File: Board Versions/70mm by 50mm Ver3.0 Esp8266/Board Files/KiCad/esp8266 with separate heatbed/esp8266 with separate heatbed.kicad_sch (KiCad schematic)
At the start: 11 parts

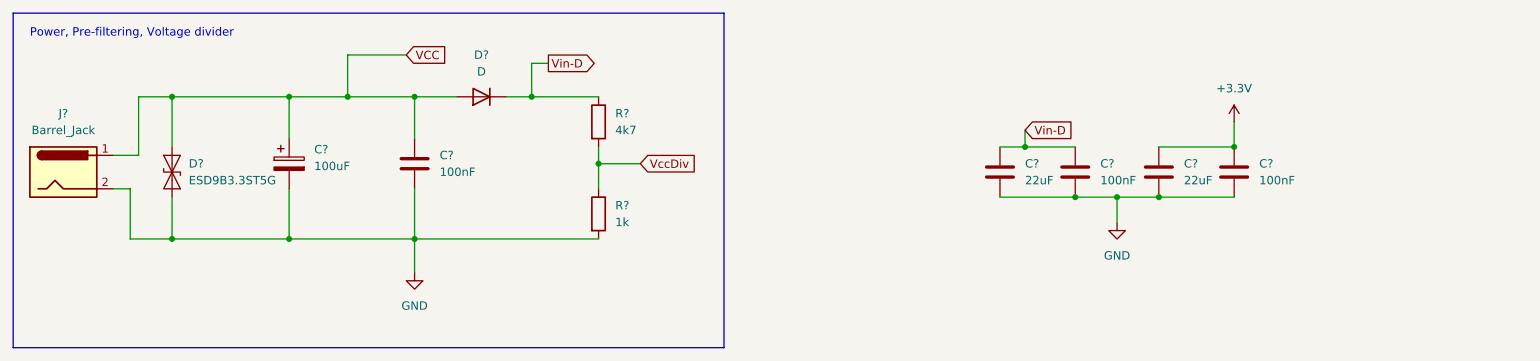
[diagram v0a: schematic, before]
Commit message: LDO + temperature
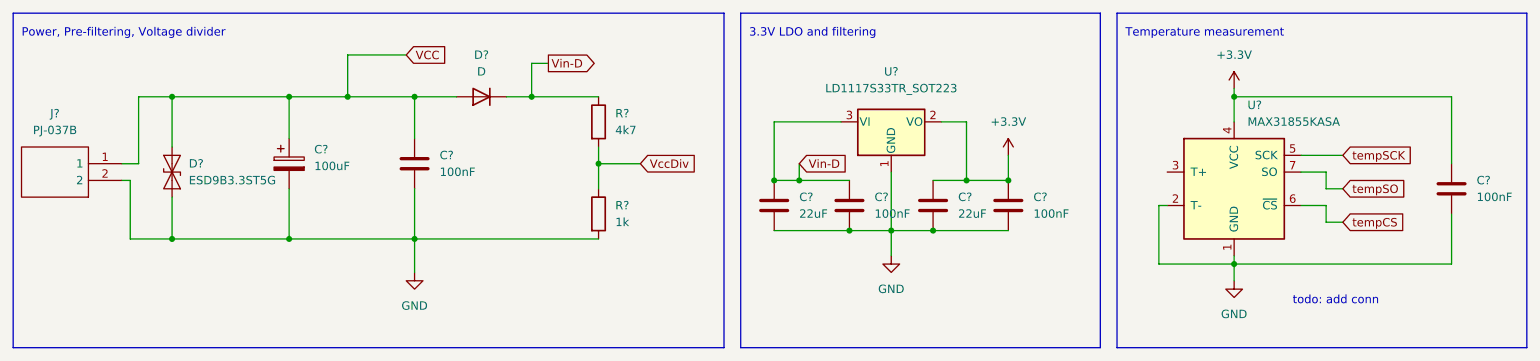
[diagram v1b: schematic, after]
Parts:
- removed J?: Barrel_Jack, symbol Connector:Barrel_Jack
- added C?: 100nF, symbol Device:C
- added J?: PJ-037B, PJ037B, symbol library_loader:PJ-037B
- added U?: LD1117S33TR_SOT223, Package_TO_SOT_SMD:SOT-223-3_TabPin2, symbol Regulator_Linear:LD1117S33TR_SOT223
- added U?: MAX31855KASA, Package_SO:SOIC-8_3.9x4.9mm_P1.27mm, symbol Sensor_Temperature:MAX31855KASA
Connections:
- net +3V3: now also C?.1, U?.2 (VO), U?.4 (VCC)
- net GND: now also C?.2, J?.2, U?.1 (GND), U?.1 (GND), U?.2 (T-)
- net VCC: now also J?.1
- net Vin-D: now also U?.3 (VI)
- new net tempCS: U?.6 (~{CS})
- new net tempSCK: U?.5 (SCK)
- new net tempSO: U?.7 (SO)
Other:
- note added: "3.3V LDO and filtering"
- note added: "Temperature measurement"
- note added: "todo: add conn"
- moved on the sheet: C?

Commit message: Some more that I don't remember
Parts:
- added C?: 1nF, symbol Device:C
- added D?: D_Zener, symbol Device:D_Zener
- added R?: 10k, symbol Device:R
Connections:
- net GND: now also R?.2
- net VCC: now also C?.1, D?.1 (K)
- new net: C?.2, D?.2 (A)
- new net Gate: R?.1
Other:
- note added: "Heatbed"
- note added: "todo: add conn + mosfet"
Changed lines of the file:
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@@
   (junction (at 77.47 49.53) (diameter 0) (color 0 0 0 0)
   )
+  (junction (at 195.58 77.47) (diameter 0) (color 0 0 0 0)
+  )
   (junction (at 156.21 48.26) (diameter 0) (color 0 0 0 0)
   )
@@
   (junction (at 135.89 40.64) (diameter 0) (color 0 0 0 0)
   )
+  (wire (pts (xy 190.5 85.09) (xy 201.93 85.09))
+    (stroke (width 0) (type default) (color 0 0 0 0))
+  )
   (wire (pts (xy 105.41 38.1) (xy 105.41 41.91))
     (stroke (width 0) (type default) (color 0 0 0 0))
@@
     (stroke (width 0) (type default) (color 0 0 0 0))
   )
+  (wire (pts (xy 204.47 97.79) (xy 204.47 100.33))
+    (stroke (width 0) (type default) (color 0 0 0 0))
+  )
   (polyline (pts (xy 184.15 66.04) (xy 246.38 66.04))
     (stroke (width 0) (type default) (color 0 0 0 0))
@@
     (stroke (width 0) (type default) (color 0 0 0 0))
   )
+  (wire (pts (xy 195.58 77.47) (xy 201.93 77.47))
+    (stroke (width 0) (type default) (color 0 0 0 0))
+  )
   (wire (pts (xy 215.9 46.99) (xy 218.44 46.99))
     (stroke (width 0) (type default) (color 0 0 0 0))
@@
     (stroke (width 0) (type default) (color 0 0 0 0))
   )
+  (wire (pts (xy 196.85 90.17) (xy 204.47 90.17))
+    (stroke (width 0) (type default) (color 0 0 0 0))
+  )
   (polyline (pts (xy 246.38 15.24) (xy 184.15 15.24))
     (stroke (width 0) (type default) (color 0 0 0 0))
@@
     (stroke (width 0) (type default) (color 0 0 0 0))
   )
+  (wire (pts (xy 190.5 77.47) (xy 195.58 77.47))
+    (stroke (width 0) (type default) (color 0 0 0 0))
+  )
   (wire (pts (xy 161.29 40.64) (xy 167.64 40.64))
     (stroke (width 0) (type default) (color 0 0 0 0))
@@
     (stroke (width 0) (type default) (color 0 0 0 0))
   )
+  (polyline (pts (xy 184.15 69.85) (xy 184.15 107.95))
+    (stroke (width 0) (type default) (color 0 0 0 0))
+  )
+  (polyline (pts (xy 245.11 107.95) (xy 184.15 107.95))
+    (stroke (width 0) (type default) (color 0 0 0 0))
+  )
   (polyline (pts (xy 127 15.24) (xy 127 66.04))
     (stroke (width 0) (type default) (color 0 0 0 0))
@@
     (stroke (width 0) (type default) (color 0 0 0 0))
   )
+  (polyline (pts (xy 245.11 69.85) (xy 245.11 107.95))
+    (stroke (width 0) (type default) (color 0 0 0 0))
+  )
   (wire (pts (xy 135.89 38.1) (xy 135.89 40.64))
     (stroke (width 0) (type default) (color 0 0 0 0))
@@
     (stroke (width 0) (type default) (color 0 0 0 0))
   )
+  (wire (pts (xy 195.58 74.93) (xy 195.58 77.47))
+    (stroke (width 0) (type default) (color 0 0 0 0))
+  )
   (wire (pts (xy 40.64 27.94) (xy 58.42 27.94))
     (stroke (width 0) (type default) (color 0 0 0 0))
@@
     (stroke (width 0) (type default) (color 0 0 0 0))
   )
+  (polyline (pts (xy 184.15 69.85) (xy 245.11 69.85))
+    (stroke (width 0) (type default) (color 0 0 0 0))
+  )
   (wire (pts (xy 215.9 39.37) (xy 215.9 41.91))
     (stroke (width 0) (type default) (color 0 0 0 0))
@@
   (wire (pts (xy 149.86 48.26) (xy 149.86 52.07))
     (stroke (width 0) (type default) (color 0 0 0 0))
+  )
+  (text "Heatbed" (at 185.42 73.66 0)
+    (effects (font (size 1.27 1.27)) (justify left bottom))
+  )
+  (text "todo: add conn + mosfet\n" (at 214.63 88.9 0)
+    (effects (font (size 1.27 1.27)) (justify left bottom))
   )
   (text "Temperature measurement" (at 185.42 19.05 0)
@@
     )
   )
-  (global_label "VCC" (shape input) (at 76.2 21.59 0) (fields_autoplaced)
+  (global_label "VCC" (shape input) (at 195.58 74.93 0) (fields_autoplaced)
+    (effects (font (size 1.27 1.27)) (justify left))
+    (property "Intersheet References" "${INTERSHEET_REFS}" (id 0) (at 201.6217 74.8506 0)
+      (effects (font (size 1.27 1.27)) (justify left) hide)
+    )
+  )
+  (global_label "VCC" (shape output) (at 76.2 21.59 0) (fields_autoplaced)
     (effects (font (size 1.27 1.27)) (justify left))
     (property "Intersheet References" "${INTERSHEET_REFS}" (id 0) (at 82.2417 21.5106 0)
@@
     )
   )
+  (global_label "Gate" (shape input) (at 196.85 90.17 180) (fields_autoplaced)
+    (effects (font (size 1.27 1.27)) (justify right))
+    (property "Intersheet References" "${INTERSHEET_REFS}" (id 0) (at 190.2036 90.0906 0)
+      (effects (font (size 1.27 1.27)) (justify right) hide)
+    )
+  )
   (global_label "Vin-D" (shape output) (at 97.79 22.86 0) (fields_autoplaced)
     (effects (font (size 1.27 1.27)) (justify left))
@@
     (pin "1")
   )
+  (symbol (lib_id "power:GND") (at 204.47 100.33 0) (unit 1)
+    (in_bom yes) (on_board yes) (fields_autoplaced)
+    (property "Reference" "#PWR?" (id 0) (at 204.47 106.68 0)
+      (effects (font (size 1.27 1.27)) hide)
+    )
+    (property "Value" "GND" (id 1) (at 204.47 105.41 0))
+    (property "Footprint" "" (id 2) (at 204.47 100.33 0)
+      (effects (font (size 1.27 1.27)) hide)
+    )
+    (property "Datasheet" "" (id 3) (at 204.47 100.33 0)
+      (effects (font (size 1.27 1.27)) hide)
+    )
+    (pin "1")
+  )
   (symbol (lib_id "power:+3.3V") (at 201.93 26.67 0) (unit 1)
     (in_bom yes) (on_board yes) (fields_autoplaced)
@@
     (pin "1")
   )
+  (symbol (lib_id "Device:D_Zener") (at 201.93 81.28 270) (unit 1)
+    (in_bom yes) (on_board yes) (fields_autoplaced)
+    (property "Reference" "D?" (id 0) (at 204.47 80.0099 90)
+      (effects (font (size 1.27 1.27)) (justify left))
+    )
+    (property "Value" "D_Zener" (id 1) (at 204.47 82.5499 90)
+      (effects (font (size 1.27 1.27)) (justify left))
+    )
+    (property "Footprint" "" (id 2) (at 201.93 81.28 0)
+      (effects (font (size 1.27 1.27)) hide)
+    )
+    (property "Datasheet" "~" (id 3) (at 201.93 81.28 0)
+      (effects (font (size 1.27 1.27)) hide)
+    )
+    (pin "1")
+    (pin "2")
+  )
   (symbol (lib_id "Device:C") (at 156.21 44.45 0) (unit 1)
     (in_bom yes) (on_board yes) (fields_autoplaced)
@@
     )
     (property "Datasheet" "~" (id 3) (at 132.08 44.45 0)
+      (effects (font (size 1.27 1.27)) hide)
+    )
+    (pin "1")
+    (pin "2")
+  )
+  (symbol (lib_id "Device:C") (at 190.5 81.28 0) (unit 1)
+    (in_bom yes) (on_board yes) (fields_autoplaced)
+    (property "Reference" "C?" (id 0) (at 194.31 80.0099 0)
+      (effects (font (size 1.27 1.27)) (justify left))
+    )
+    (property "Value" "1nF" (id 1) (at 194.31 82.5499 0)
+      (effects (font (size 1.27 1.27)) (justify left))
+    )
+    (property "Footprint" "" (id 2) (at 191.4652 85.09 0)
+      (effects (font (size 1.27 1.27)) hide)
+    )
+    (property "Datasheet" "~" (id 3) (at 190.5 81.28 0)
       (effects (font (size 1.27 1.27)) hide)
     )
@@
     )
     (property "Datasheet" "~" (id 3) (at 105.41 31.75 0)
+      (effects (font (size 1.27 1.27)) hide)
+    )
+    (pin "1")
+    (pin "2")
+  )
+  (symbol (lib_id "Device:R") (at 204.47 93.98 0) (unit 1)
+    (in_bom yes) (on_board yes) (fields_autoplaced)
+    (property "Reference" "R?" (id 0) (at 207.01 92.7099 0)
+      (effects (font (size 1.27 1.27)) (justify left))
+    )
+    (property "Value" "10k" (id 1) (at 207.01 95.2499 0)
+      (effects (font (size 1.27 1.27)) (justify left))
+    )
+    (property "Footprint" "" (id 2) (at 202.692 93.98 90)
+      (effects (font (size 1.27 1.27)) hide)
+    )
+    (property "Datasheet" "~" (id 3) (at 204.47 93.98 0)
       (effects (font (size 1.27 1.27)) hide)
     )
@@
       (reference "#PWR?") (unit 1) (value "GND") (footprint "")
     )
+    (path "/149494d7-0bc1-443d-9d25-3faaebebceda"
+      (reference "#PWR?") (unit 1) (value "GND") (footprint "")
+    )
     (path "/272d4c9c-5b4d-4249-af66-c174a51077dd"
       (reference "#PWR?") (unit 1) (value "+3.3V") (footprint "")
@@
       (reference "C?") (unit 1) (value "22uF") (footprint "")
     )
+    (path "/466d01e2-ff1e-4839-a77a-096609667bd7"
+      (reference "C?") (unit 1) (value "1nF") (footprint "")
+    )
     (path "/49818e0e-06f2-4b91-9eb1-6af47a9bf69c"
       (reference "C?") (unit 1) (value "100nF") (footprint "")
@@
       (reference "C?") (unit 1) (value "100nF") (footprint "")
     )
+    (path "/30f08f5d-31c5-4e32-9973-be8bdfbbe09e"
+      (reference "D?") (unit 1) (value "D_Zener") (footprint "")
+    )
     (path "/74383a9a-9fb0-4eb2-95d8-0d39d92a7c66"
       (reference "D?") (unit 1) (value "D") (footprint "")
@@
       (reference "R?") (unit 1) (value "4k7") (footprint "")
     )
+    (path "/d53dadad-9b16-4d15-aecb-0759b966964f"
+      (reference "R?") (unit 1) (value "10k") (footprint "")
+    )
     (path "/db94c8fc-a32f-4093-9a65-a86b21b63695"

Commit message: Switches
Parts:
- added R? (x2): 10k, symbol Device:R
- added S? (x2): RKC2SJF170SMTR_LFS, RKC2SJF170SMTRLFS, symbol library_loader:RKC2SJF170SMTR_LFS
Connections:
- net +3V3: now also S?.1 (COM_1), S?.1 (COM_1), S?.2 (COM_2), S?.2 (COM_2)
- net GND: now also R?.2, R?.2
- new net FLASH: R?.1, S?.3 (NO_1), S?.4 (NO_2)
- new net RESET: R?.1, S?.3 (NO_1), S?.4 (NO_2)
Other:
- note added: "Programming"
